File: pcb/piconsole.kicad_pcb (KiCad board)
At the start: 2 copper layers, 67.3 x 80.6 mm, 28 parts, among them J1 Bat, J2 GPIO, SW1 Up, SW2 Down, SW3 Left, SW4 Right, SW5 A, SW6 B, SW7 SW_SPDT, SW8 RESET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

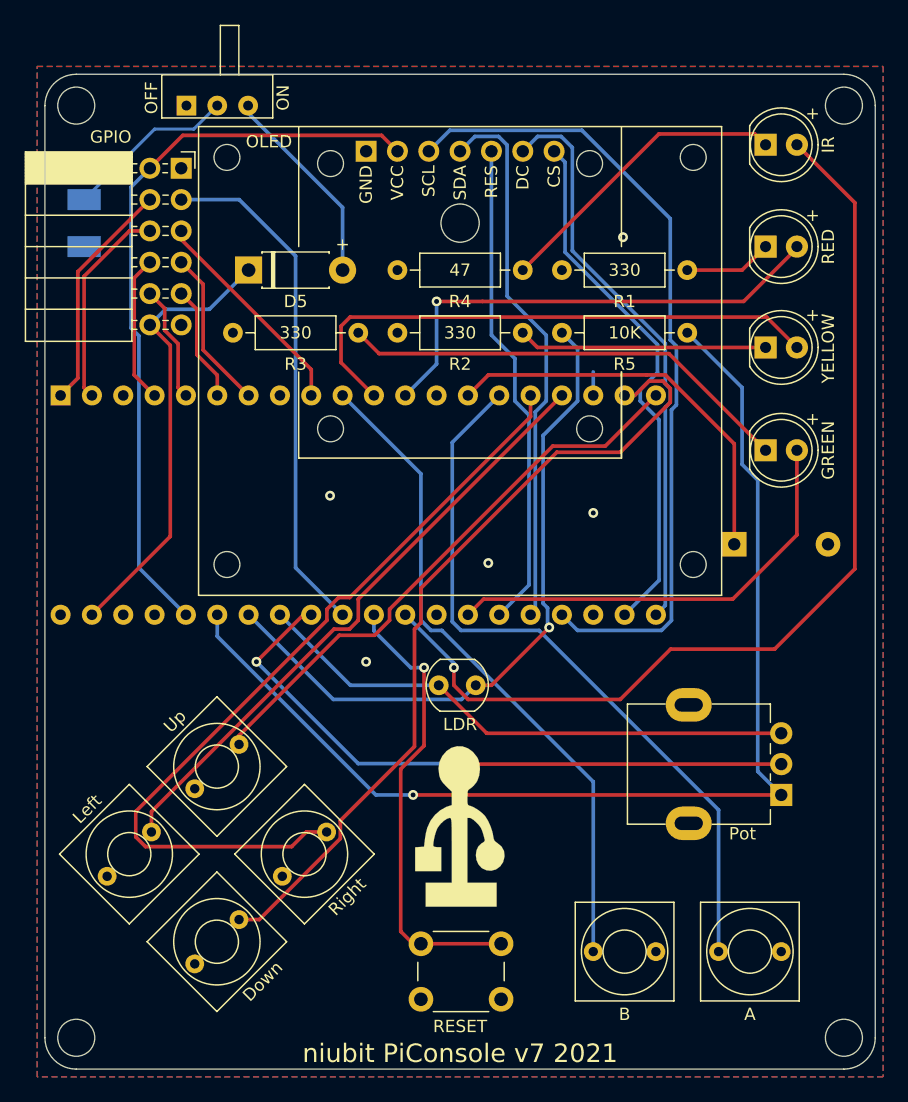
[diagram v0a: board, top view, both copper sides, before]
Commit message: Adaptado a KiCad 6.
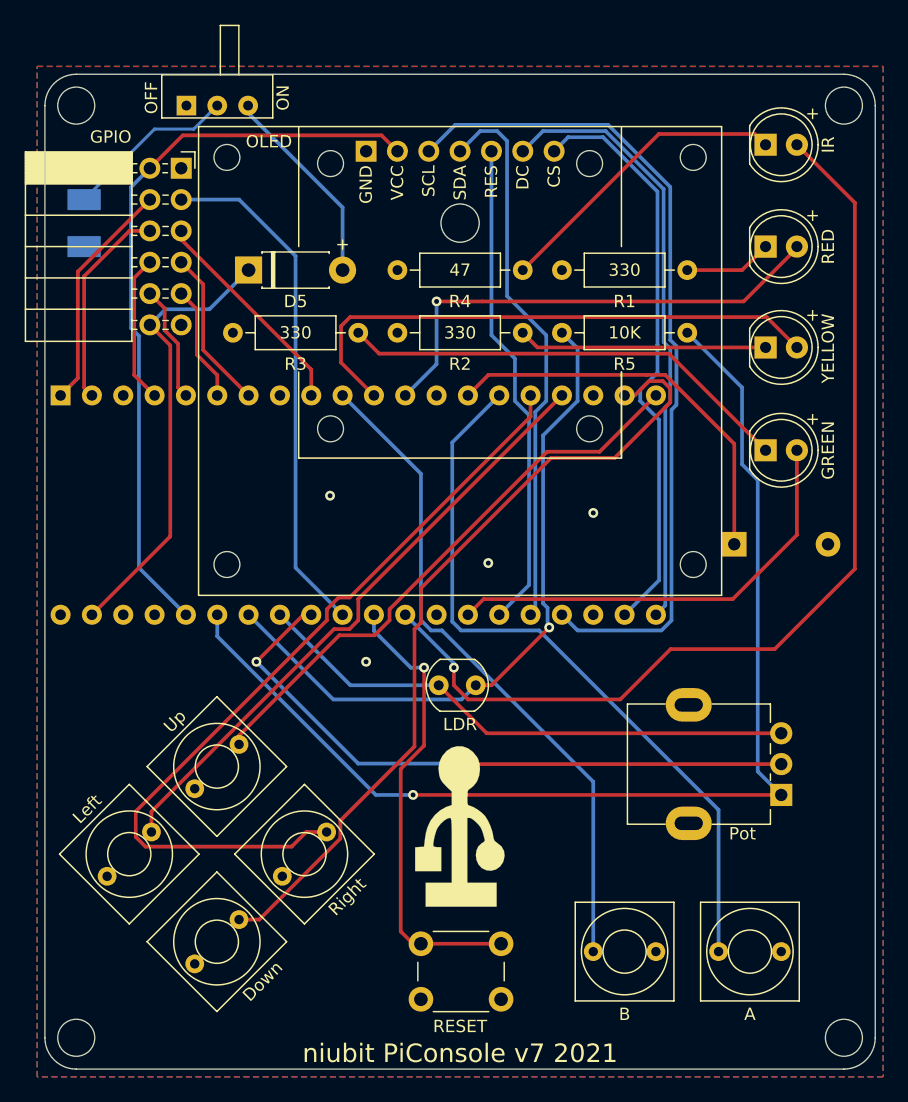
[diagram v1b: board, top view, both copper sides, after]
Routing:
- net OLED_CS: track 43.4 -> 47.3 mm
- net OLED_DC: track 46.5 -> 49.3 mm
- net GND: track 1.90 -> 0.00 mm, vias 5 -> 4
- net OLED_SCL: track 65.9 -> 67.8 mm
- net RESET: track 38.0 -> 37.3 mm
- net GP4: track 10.1 -> 9.46 mm
- net OLED_SDA: track 44.5 -> 45.1 mm
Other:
- net class Default removed

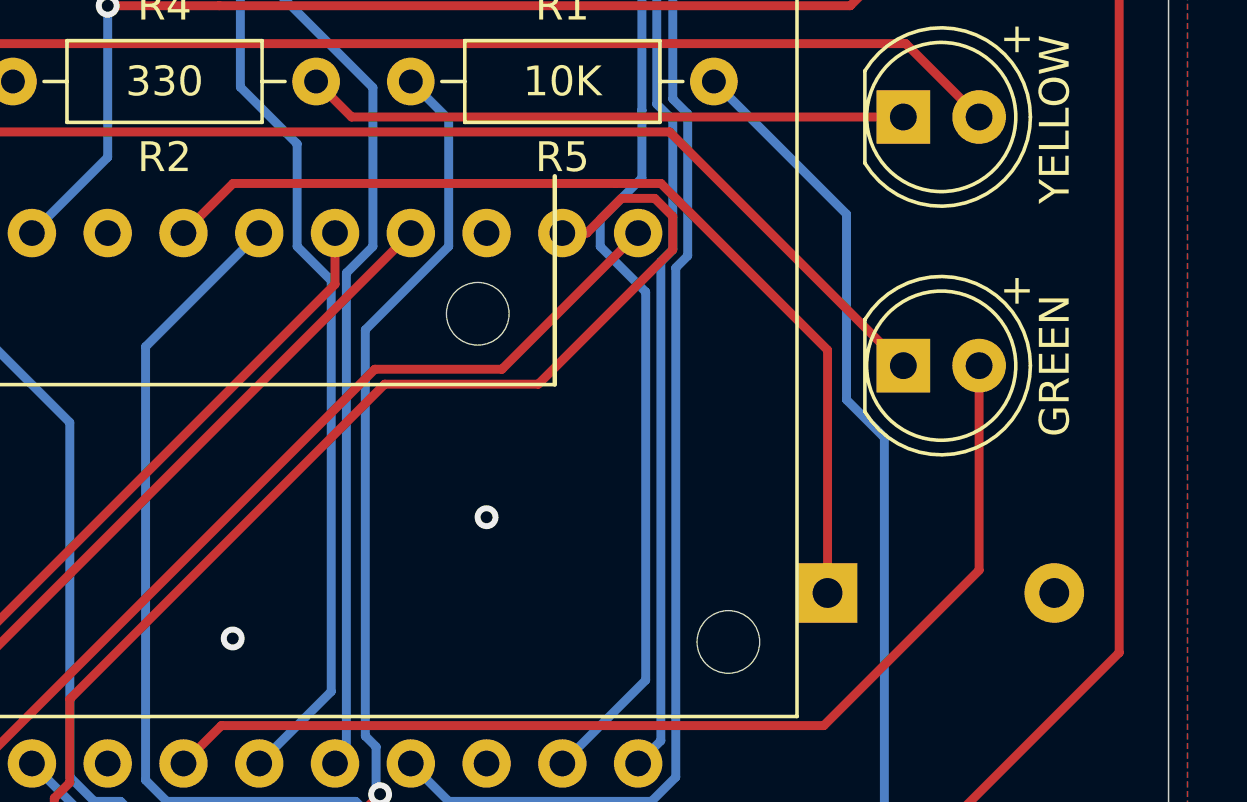
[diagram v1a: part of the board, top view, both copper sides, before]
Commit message: Nueva v7 (aún no se había fabricado)
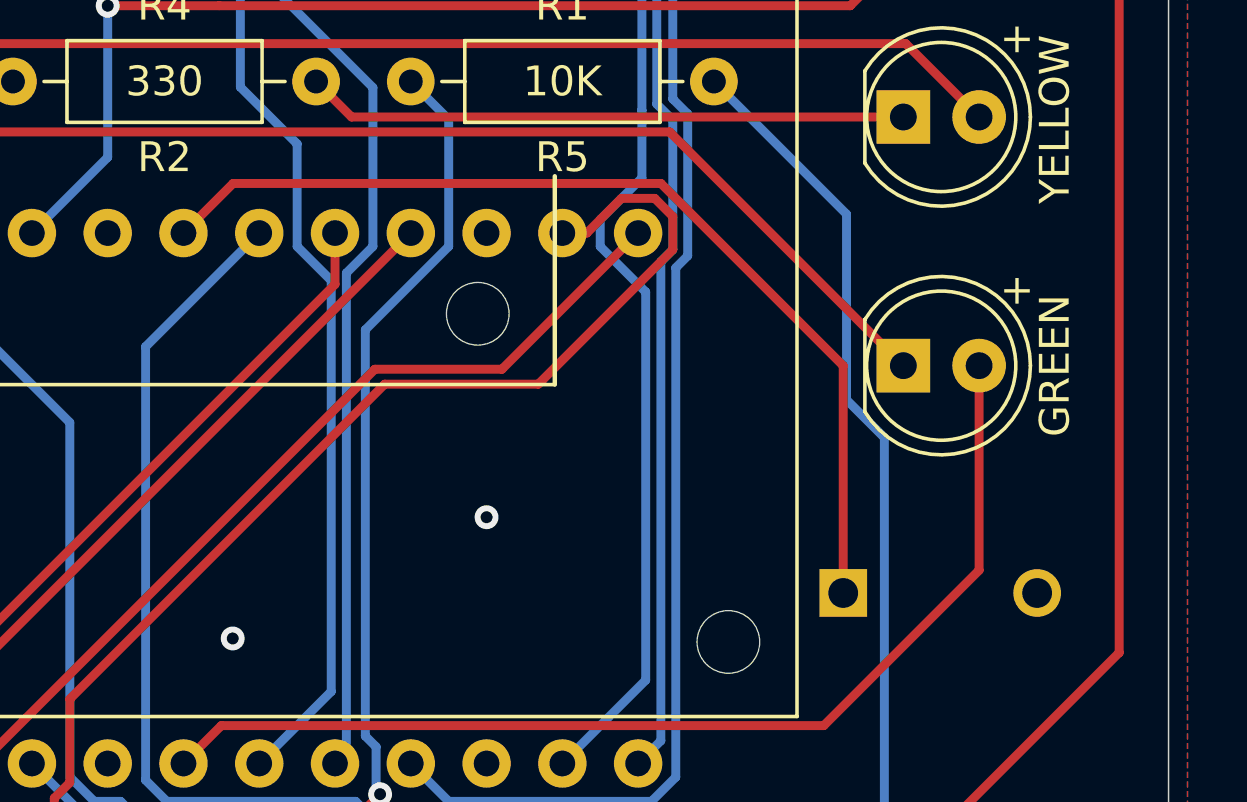
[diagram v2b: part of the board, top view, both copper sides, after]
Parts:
- BZ1: footprint Buzzer_Beeper:Buzzer_12x9.5RM7.6 -> Buzzer_Beeper:MagneticBuzzer_ProSignal_ABT-410-RC
- moved BZ1 0.53 mm to (153.6, 95.9)
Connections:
- SW7 pad 1: Net-(SW7-Pad1) -> unconnected-(SW7-Pad1)
- U1 pad 37: Net-(U1-Pad37) -> unconnected-(U1-Pad37)
- U1 pad 40: Net-(U1-Pad40) -> unconnected-(U1-Pad40)

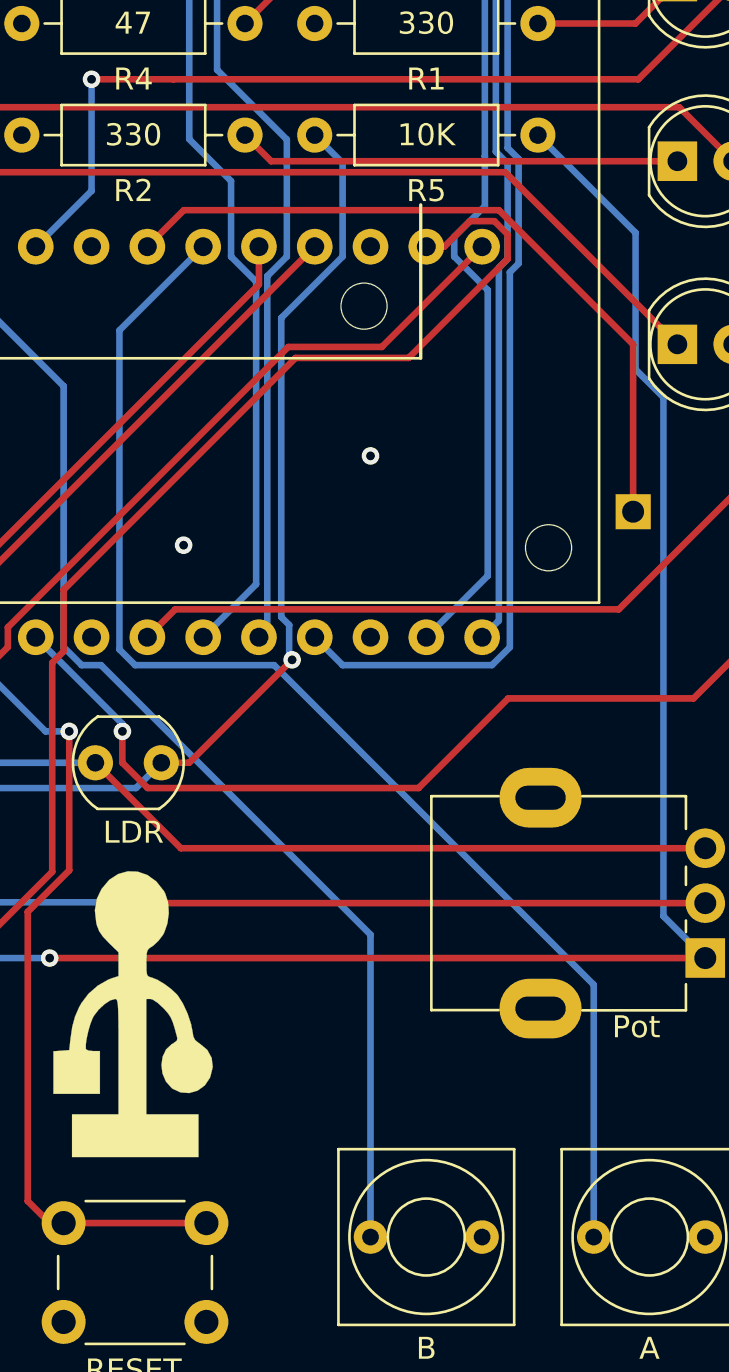
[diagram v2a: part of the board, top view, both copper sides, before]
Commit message: Se separa una via de un par
Estaba demasiado próxima.
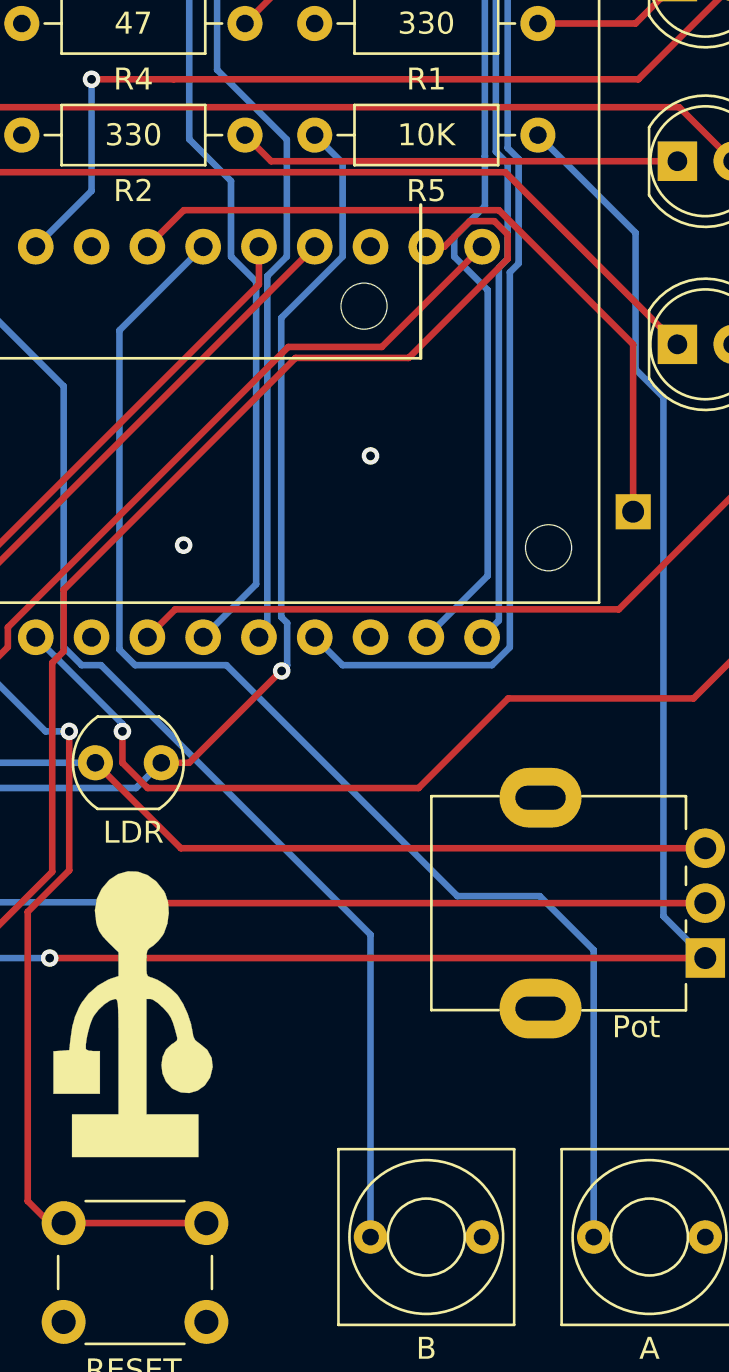
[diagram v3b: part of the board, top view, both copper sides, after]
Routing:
- net SW_A: track 59.3 -> 60.2 mm
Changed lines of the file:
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@@
   (segment (start 123.984998 116.205) (end 111.125 103.345002) (width 0.3) (layer "B.Cu") (net 15))
   (segment (start 111.125 103.345002) (end 111.125 101.6) (width 0.3) (layer "B.Cu") (net 15))
-  (segment (start 132.08 107.315) (end 133.349999 107.315) (width 0.3) (layer "F.Cu") (net 16))
-  (segment (start 133.349999 107.315) (end 138.036167 102.628832) (width 0.3) (layer "F.Cu") (net 16))
-  (via (at 138.036167 102.628832) (size 0.8) (drill 0.4) (layers "F.Cu" "B.Cu") (net 16))
-  (segment (start 140.335 80.01) (end 140.335 84.269762) (width 0.3) (layer "B.Cu") (net 16))
-  (segment (start 137.541 87.063762) (end 137.541 100.68024) (width 0.3) (layer "B.Cu") (net 16))
-  (segment (start 137.902999 101.042239) (end 137.902999 102.495664) (width 0.3) (layer "B.Cu") (net 16))
+  (segment (start 137.529999 103.135) (end 133.349999 107.315) (width 0.3) (layer "F.Cu") (net 16))
+  (segment (start 137.56 103.135) (end 137.529999 103.135) (width 0.3) (layer "F.Cu") (net 16))
+  (segment (start 133.349999 107.315) (end 132.08 107.315) (width 0.3) (layer "F.Cu") (net 16))
+  (via (at 137.56 103.135) (size 0.8) (drill 0.4) (layers "F.Cu" "B.Cu") (net 16))
+  (segment (start 137.81 100.94924) (end 137.541 100.68024) (width 0.3) (layer "B.Cu") (net 16))
   (segment (start 120.530001 108.465001) (end 113.665 101.6) (width 0.3) (layer "B.Cu") (net 16))
-  (segment (start 139.065 78.74) (end 140.335 80.01) (width 0.3) (layer "B.Cu") (net 16))
-  (segment (start 137.541 100.68024) (end 137.902999 101.042239) (width 0.3) (layer "B.Cu") (net 16))
-  (segment (start 140.335 84.269762) (end 137.541 87.063762) (width 0.3) (layer "B.Cu") (net 16))
-  (segment (start 137.902999 102.495664) (end 138.036167 102.628832) (width 0.3) (layer "B.Cu") (net 16))
+  (segment (start 137.81 102.885) (end 137.81 100.94924) (width 0.3) (layer "B.Cu") (net 16))
+  (segment (start 137.56 103.135) (end 137.81 102.885) (width 0.3) (layer "B.Cu") (net 16))
+  (segment (start 140.335 84.269762) (end 140.335 80.01) (width 0.3) (layer "B.Cu") (net 16))
   (segment (start 132.08 107.315) (end 130.929999 108.465001) (width 0.3) (layer "B.Cu") (net 16))
+  (segment (start 137.541 100.68024) (end 137.541 87.063762) (width 0.3) (layer "B.Cu") (net 16))
+  (segment (start 140.335 80.01) (end 139.065 78.74) (width 0.3) (layer "B.Cu") (net 16))
+  (segment (start 137.541 87.063762) (end 140.335 84.269762) (width 0.3) (layer "B.Cu") (net 16))
   (segment (start 130.929999 108.465001) (end 120.530001 108.465001) (width 0.3) (layer "B.Cu") (net 16))
   (segment (start 132.97 111.205) (end 129.08 107.315) (width 0.3) (layer "F.Cu") (net 17))
@@
   (segment (start 99.822 73.787) (end 105.664 67.945) (width 0.3) (layer "F.Cu") (net 37))
   (segment (start 98.425 83.82) (end 99.822 82.423) (width 0.3) (layer "F.Cu") (net 37))
-  (segment (start 151.765 117.418341) (end 137.216659 102.87) (width 0.3) (layer "B.Cu") (net 38))
-  (segment (start 137.216659 102.87) (end 130.887239 102.87) (width 0.3) (layer "B.Cu") (net 38))
+  (segment (start 135.045 102.87) (end 130.887239 102.87) (width 0.3) (layer "B.Cu") (net 38))
   (segment (start 130.887239 102.87) (end 130.175 102.157761) (width 0.3) (layer "B.Cu") (net 38))
   (segment (start 130.175 102.157761) (end 130.175 87.63) (width 0.3) (layer "B.Cu") (net 38))
-  (segment (start 151.765 128.905) (end 151.765 117.418341) (width 0.3) (layer "B.Cu") (net 38))
   (segment (start 130.175 87.63) (end 133.985 83.82) (width 0.3) (layer "B.Cu") (net 38))
+  (segment (start 151.765 115.84) (end 149.31 113.385) (width 0.3) (layer "B.Cu") (net 38))
+  (segment (start 151.765 128.905) (end 151.765 115.84) (width 0.3) (layer "B.Cu") (net 38))
+  (segment (start 145.56 113.385) (end 135.045 102.87) (width 0.3) (layer "B.Cu") (net 38))
+  (segment (start 149.31 113.385) (end 145.56 113.385) (width 0.3) (layer "B.Cu") (net 38))
   (segment (start 141.605 128.905) (end 141.605 115.137998) (width 0.3) (layer "B.Cu") (net 39))
   (segment (start 129.337002 102.87) (end 128.455238 102.87) (width 0.3) (layer "B.Cu") (net 39))
